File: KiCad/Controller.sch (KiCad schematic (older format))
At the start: 22 parts, among them CON401 AVR_ISP, J401 Power, J402 Power, J403 Power, J404 Port D, J405 Port B, J406 Port C, J407 ADC6, J408 ADC7, U401 ATMEGA88A-AU, Y401 20MHz

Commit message: Schematic Version 4 Some Software Changes
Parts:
- removed C403, C404, C405, C407: 100n, Capacitors_SMD:C_0805, symbol C
- removed J401: Power, Socket_Strips:Socket_Strip_Straight_2x03, symbol Conn_02x03_Odd_Even
- removed J402: Power, Socket_Strips:Socket_Strip_Straight_2x04, symbol Conn_02x04_Odd_Even
- removed J403: Power, Socket_Strips:Socket_Strip_Straight_2x05, symbol Conn_02x05_Odd_Even
- removed J404: Port D, Socket_Strips:Socket_Strip_Straight_1x03, symbol Conn_01x03
- removed J405: Port B, Socket_Strips:Socket_Strip_Straight_1x04, symbol Conn_01x04
- removed J406: Port C, Socket_Strips:Socket_Strip_Straight_1x05, symbol Conn_01x05
- added C? (x3): 100n, Capacitors_SMD:C_0805, symbol C
- added J?: Power B, symbol Conn_02x06_Odd_Even
- added J?: Port B, symbol Conn_01x06
- added J?: Conn_01x04, symbol Conn_01x04
- C408, C409: Populate Prototype -> (none)
- CON401: footprint Pin_Headers:Pin_Header_Straight_2x03 -> Connectors_IDC:IDC-Header_2x03_Pitch2.54mm_Straight
- J407, J408: Assembly (none) -> DNP
- Y401: footprint Crystals:Crystal_HC49-SD_SMD -> Crystals:Crystal_SMD_HC49-SD; Populate Prototype -> (none)
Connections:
- net labels added: PB1, PB2, RGB_D
- net labels removed: PC1, PC2, PC3, PC4, PC5, PWM_B, PWM_G, PWM_R
- wire segments 113 -> 95
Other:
- note added: "Bei 20MHz ist ein Bit für die LEDs genau 25 (max. 37) Takte lang.\n"
- note removed: "Hier kann ggf ein 20 MHz \nQuarz genutzt werden.\nInterner RC Oszillator: \n8MHz±10% (±2% kalibriert)"
- moved on the sheet: C402, J407, J408

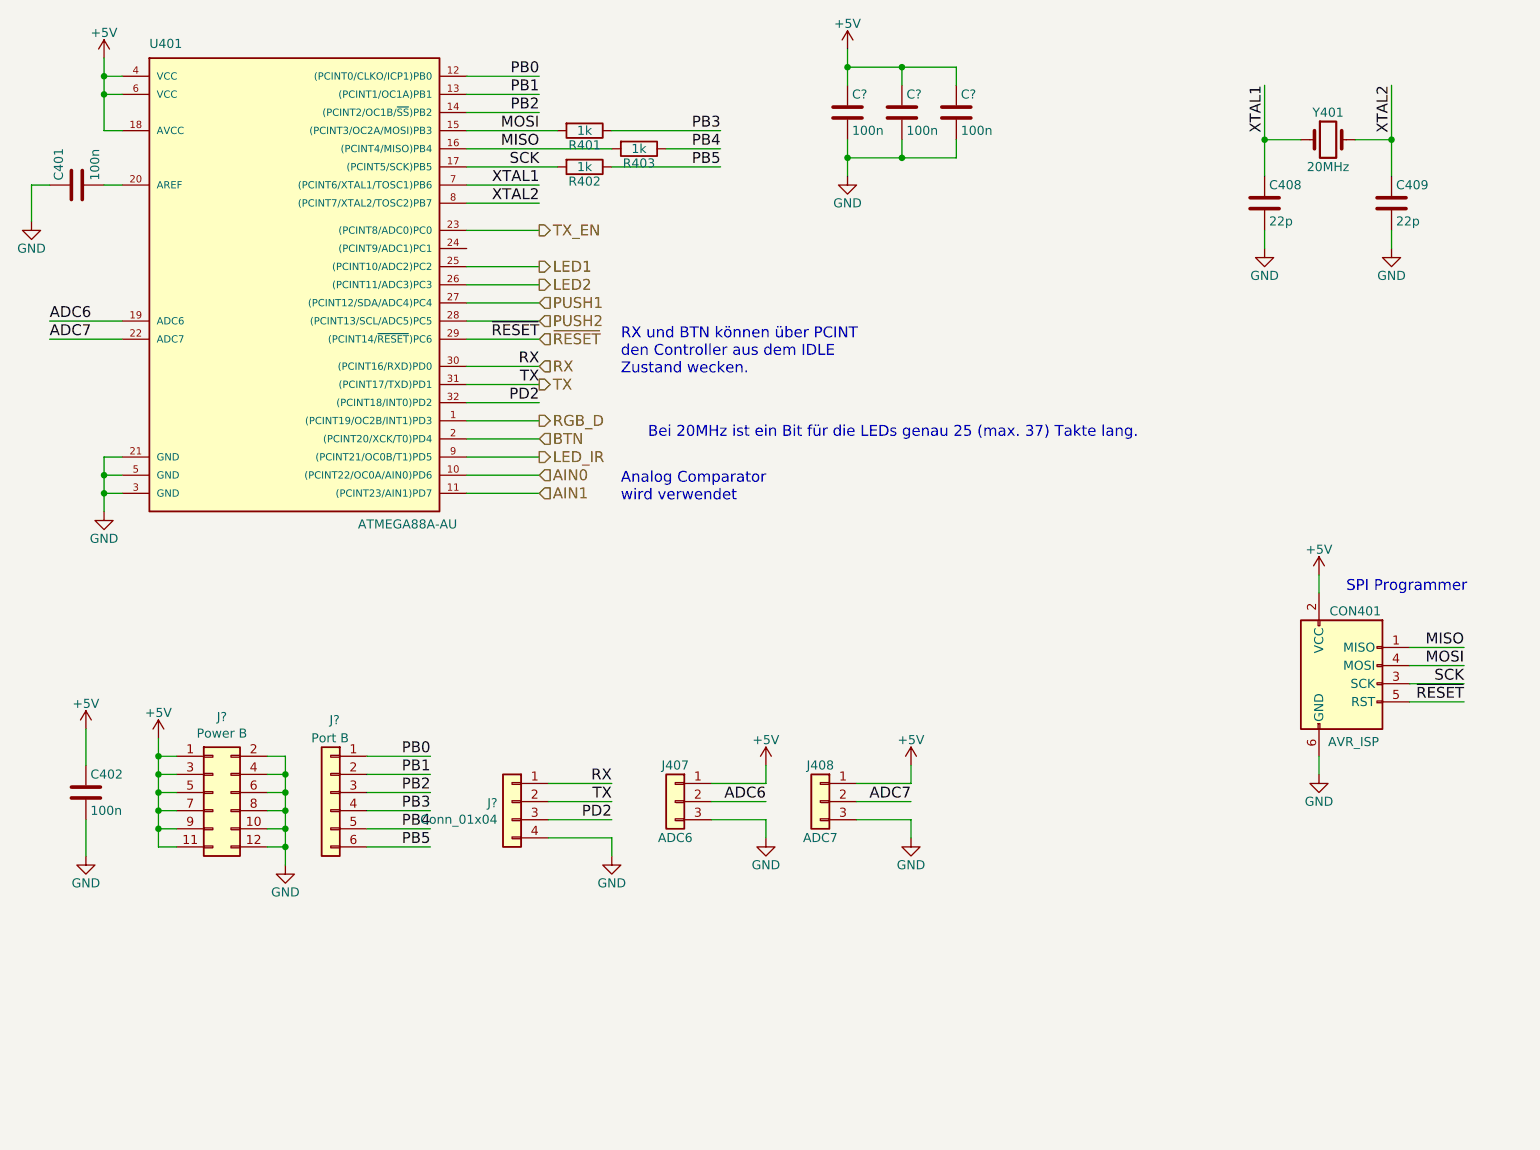
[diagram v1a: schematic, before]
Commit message: Changes to V4 Schematic, new Board design
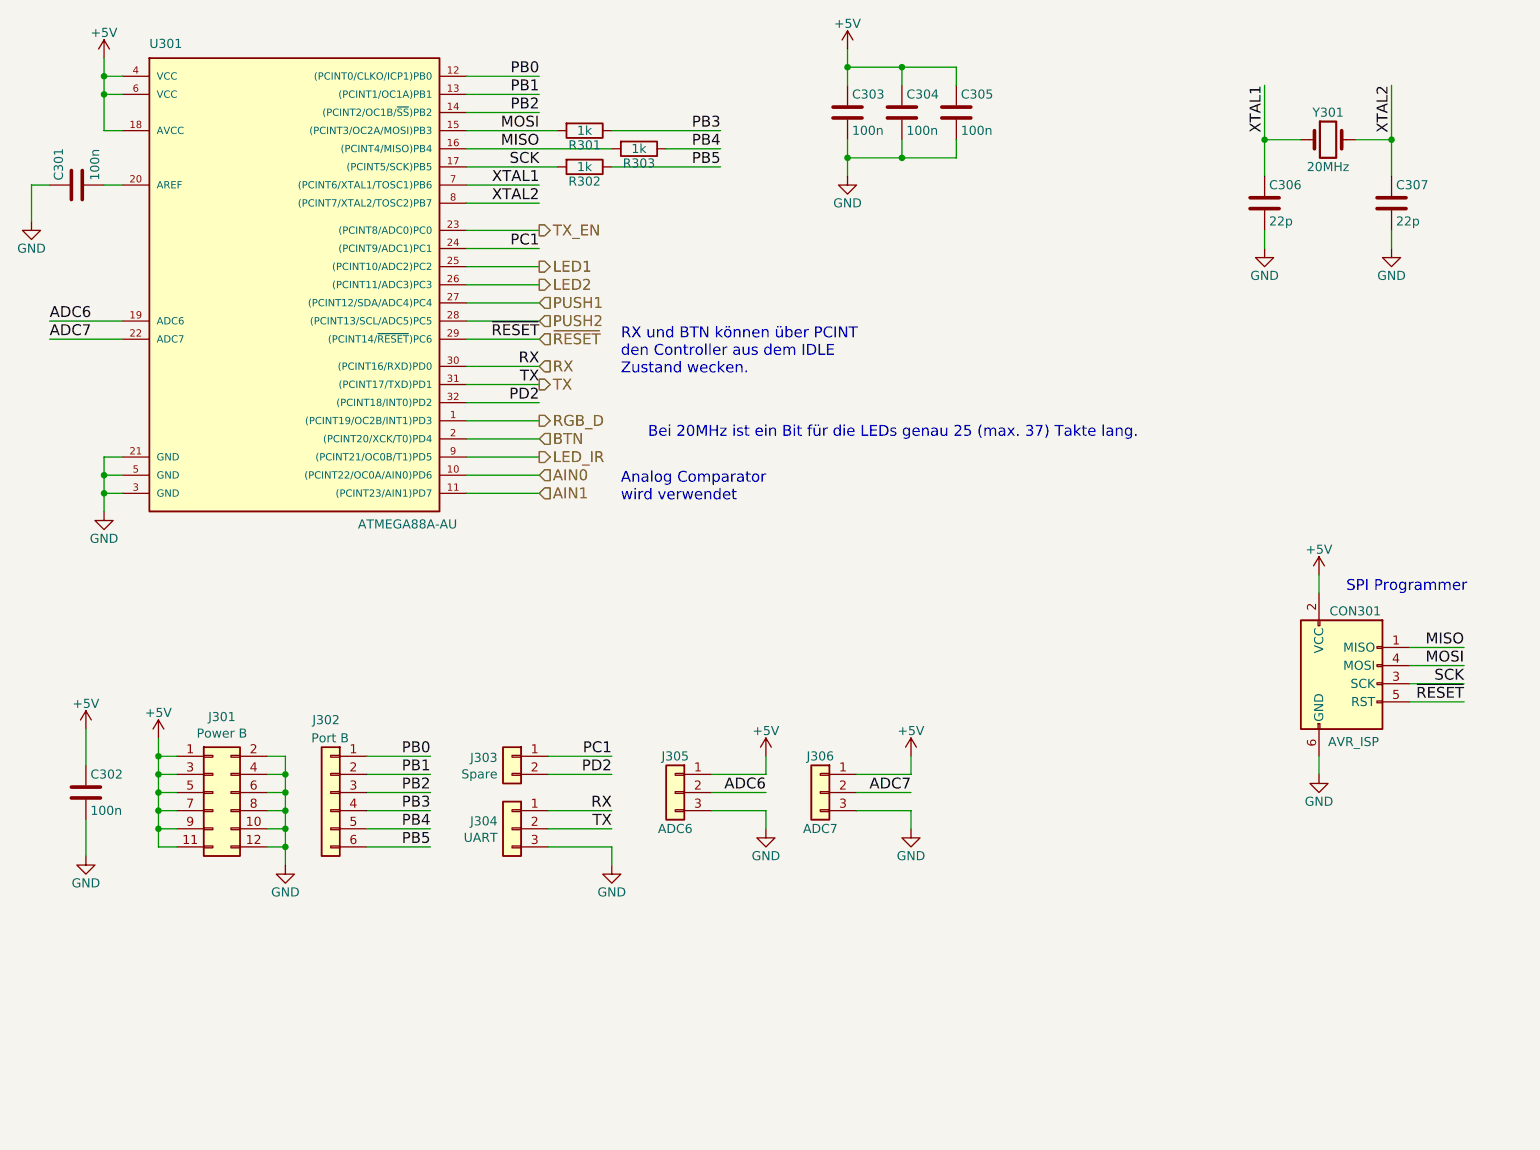
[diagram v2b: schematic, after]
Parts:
- removed J?: Conn_01x04, symbol Conn_01x04
- added J303: Spare, Socket_Strips:Socket_Strip_Straight_1x02_Pitch2.54mm, symbol Conn_01x02
- added J304: UART, Socket_Strips:Socket_Strip_Straight_1x03_Pitch2.54mm, symbol Conn_01x03
- J301: renamed from J?; footprint (none) -> Socket_Strips:Socket_Strip_Straight_2x06_Pitch2.54mm
- J302: renamed from J?; footprint (none) -> Socket_Strips:Socket_Strip_Straight_1x06_Pitch2.54mm
- J305: renamed from J407; footprint Socket_Strips:Socket_Strip_Straight_1x03 -> Socket_Strips:Socket_Strip_Straight_1x03_Pitch2.54mm
- J306: renamed from J408; footprint Socket_Strips:Socket_Strip_Straight_1x03 -> Socket_Strips:Socket_Strip_Straight_1x03_Pitch2.54mm
- Y301: renamed from Y401; footprint Crystals:Crystal_SMD_HC49-SD -> Crystals:Crystal_HC49-U_Vertical
- gave numbers to parts that had none: 3
- renumbered C401 to C301, C402 to C302, C408 to C306, C409 to C307, CON401 to CON301, R401 to R301, R402 to R302, R403 to R303, U401 to U301
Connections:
- net GND: now also J304.3 (Pin_3)
- net PD2: now also J303.2 (Pin_2)
- net RX: now also J304.1 (Pin_1)
- net TX: now also J304.2 (Pin_2)
- net PC1: now reaches U301.24 ((PCINT9/ADC1)PC1)
- net PC1: now also J303.1 (Pin_1)
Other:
- moved on the sheet: J305, J306

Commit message: Version 4 Shift Register
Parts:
- J301, J302, J303, J304: Assembly (none) -> DNP
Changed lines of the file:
@@
 F 2 "Socket_Strips:Socket_Strip_Straight_2x06_Pitch2.54mm" H 2100 5400 50  0001 C CNN
 F 3 "~" H 2100 5400 50  0001 C CNN
+F 4 "DNP" H 2100 5400 60  0001 C CNN "Assembly"
 	1    2100 5400
 	1    0    0    -1
@@
 F 2 "Socket_Strips:Socket_Strip_Straight_1x06_Pitch2.54mm" H 2750 5400 50  0001 C CNN
 F 3 "~" H 2750 5400 50  0001 C CNN
+F 4 "DNP" H 2750 5400 60  0001 C CNN "Assembly"
 	1    2750 5400
 	-1   0    0    -1
@@
 F 2 "Socket_Strips:Socket_Strip_Straight_1x03_Pitch2.54mm" H 3750 5600 50  0001 C CNN
 F 3 "~" H 3750 5600 50  0001 C CNN
+F 4 "DNP" H 3750 5600 60  0001 C CNN "Assembly"
 	1    3750 5600
 	-1   0    0    -1
@@
 F 2 "Socket_Strips:Socket_Strip_Straight_1x02_Pitch2.54mm" H 3750 5200 50  0001 C CNN
 F 3 "~" H 3750 5200 50  0001 C CNN
+F 4 "DNP" H 3750 5200 60  0001 C CNN "Assembly"
 	1    3750 5200
 	-1   0    0    -1
